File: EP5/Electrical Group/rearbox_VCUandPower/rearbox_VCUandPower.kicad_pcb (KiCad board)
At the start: 2 copper layers, 148.9 x 79.5 mm, 245 parts, among them IC1 MCP6C04T-100E_CHY, IC2 LMR14050SDDAR, IC3 MCP6C04T-100E_CHY, IC4 LD39100PU33RY, IC5 TCAN1057AVDRQ1, IC6 LMR50410Y3FQDBVRQ1, J1 JTAG, J10 24V_raw, J11 24V_raw, J12 5V external, J13 USBC_RPI_5VOnly, J14 USBA_RPI_5Vonly, J15 fan1, J16 fan2, J17 UPS_cap, J18 5Vout, J19 Rpi, J2 MSD-4-A, J20 GPS_UART, J21 3V3out, J22 CAN_termination, J23 CAN, J24 left connector, J25 rear_connector, J26 buzzer, J27 I2C, J3 USB_OTG, J4 LVBattery, J5 GLVMS, J6 GPVMP, J7 24V_noisy1, J8 24V_noisy1, J9 24V_noisy1, Q1 SI3407, SW1 BOOT0, SW2 VBUS, SW3 NRST, U1 STM32H562VGTx, U2 USBLC6-2SC6, U3 LM2903, U4 MAX487E, U5 MAX487E, U6 74HC595, U7 74HC595, U8 SM420561N, U9 SM420561N, Y1 24MHz, Y2 32.768kHz

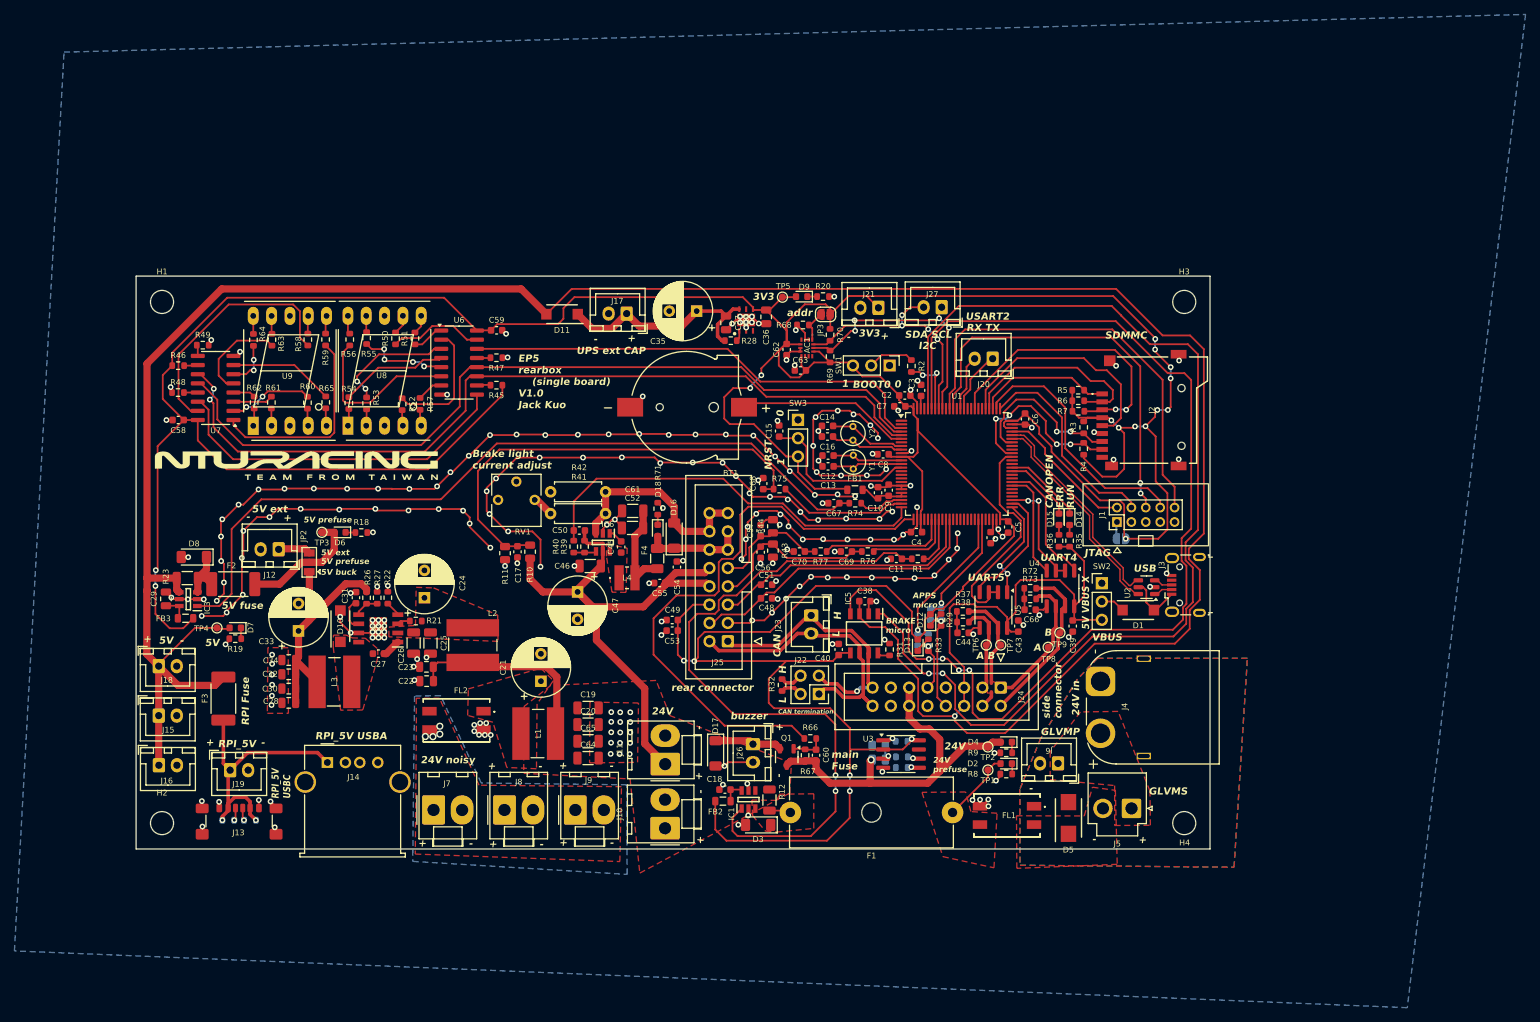
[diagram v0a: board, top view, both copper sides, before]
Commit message: add rearbox_VCUandPower to EP5
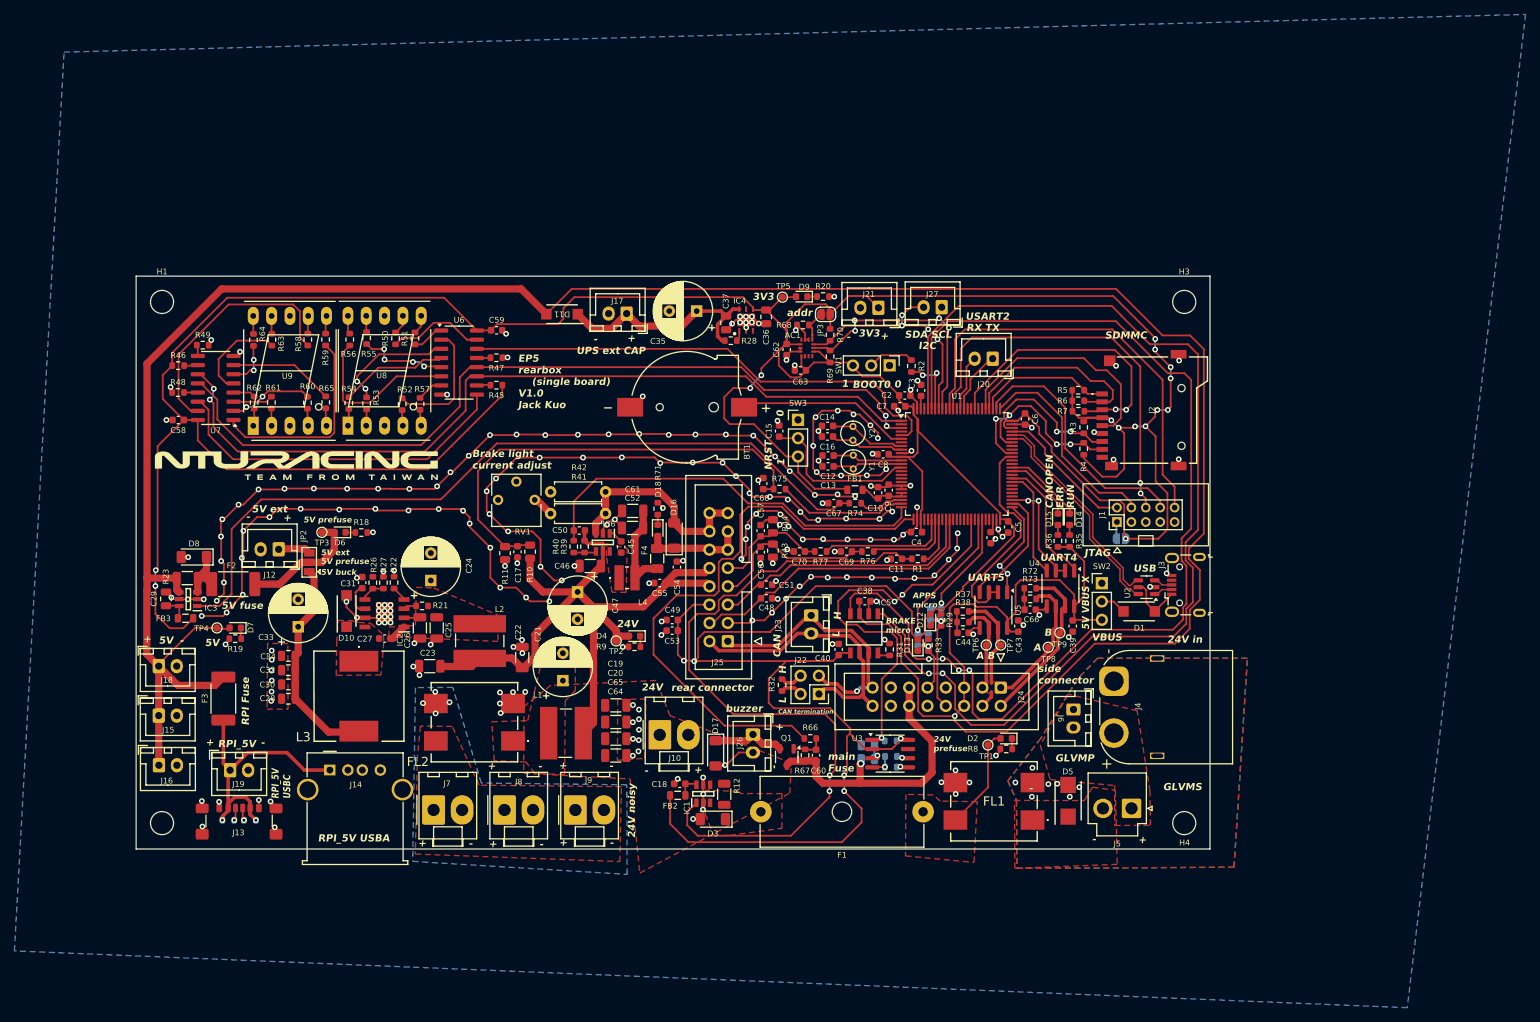
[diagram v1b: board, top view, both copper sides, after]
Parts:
- removed J11: 24V_raw, Connector_Molex:Molex_KK-396_A-41791-0002_1x02_P3.96mm_Vertical
- AC1: value LSM6DSOXTR -> LSM6DSO32
- C1, C3: value 2.2u 16V -> 2u2 16V
- C11, C67, C68, C69, C70: value 0u1 -> 1u
- C19, C20, C64, C65: value 1u 35V -> 10u 35V
- C22, C23: value 1u 35V -> 10u 35V; footprint Capacitor_SMD:C_0805_2012Metric -> Capacitor_SMD:C_1206_3216Metric
- C29: value 1u 16V -> 10u 16V
- D1, D10, D11: value 45V 2A (VSSAF5L45HM3_A_H) -> 45V 3A (VSSAF5L45HM3_A_H)
- F2: value 1A -> 3A
- F4: value 0.5A -> 1A
- FL1, FL2: value SRF0905A-202Y -> ACM12V-351-2PL-TL00; footprint SamacSys_Parts:SRF0905A102Y -> SamacSys_Parts:ACM12V3512PLTL00
- L1: value ?uH 10A () -> 1.5uH 10A (SRP6530A-1R5M)
- L2: value ?uH 1A -> 18uH 1.5A (SRR6040A-180M)
- L3: value 18uF 1A (SRR6040A-180M) -> 22uH 4A (SRR1260A-220M); footprint SamacSys_Parts:SRR6040A180M -> SamacSys_Parts:SRR1260A220M
- R13: value 100k -> 270k
- R43, R44: value 150R 1% -> 120R 1%
- R74, R75, R76, R77: value 1k -> 10k
- moved R9 53.6 mm to (128.3, 106.5)
- moved TP2 53.6 mm to (125.8, 105.7)
- moved D4 53.6 mm to (128.3, 105.0)
- moved C22 13.7 mm to (112.7, 108.0), turned to 90 degrees
- moved J10 13.0 mm to (131.8, 118.7), turned to 0 degrees
- moved J6 7.78 mm to (189.2, 115.2), turned to -90 degrees
- moved D3 6.32 mm to (139.2, 130.4)
- moved IC1 6.32 mm to (137.8, 126.9)
- moved C18 6.32 mm to (134.6, 125.5)
- moved FB2 6.32 mm to (134.3, 127.1)
- moved R12 6.32 mm to (140.7, 126.9)
- moved F1 4.09 mm to (168.3, 129.4)
- moved L3 3.93 mm to (90.1, 113.3), turned to 0 degrees
- moved C19 3.87 mm to (125.7, 114.6)
- moved C65 3.87 mm to (125.7, 119.2)
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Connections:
- net /SCL1_SCL renamed /I2C1_SCL
- net /SCL1_SDA renamed /I2C1_SDA
- FL1 pad 1: GNDPWR -> /power/+24V_preCMfilter
- FL1 pad 2: /power/+24V_preCMfilter -> GNDPWR
- FL1 pad 3: /power/+24V_proCMfilter -> GND
- FL1 pad 4: GND -> /power/+24V_proCMfilter
- U1 pad 1: /SPI4_MISO -> /SPI4_SCK
- U1 pad 3: /SPI4_MOSI -> /SPI4_CS
- U1 pad 4: /SPI4_CS -> /SPI4_MISO
- U1 pad 42: unconnected-(U1-PE11-Pad42) -> /24V_lowTrig
- U1 pad 5: /SPI4_SCK -> /SPI4_MOSI
- U1 pad 57: /UART4_TX -> unconnected-(U1-PD10-Pad57)
- U1 pad 58: /UART4_RX -> /UART4_TX
- U1 pad 59: unconnected-(U1-PD12-Pad59) -> /UART4_RX
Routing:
- net /24V_lowTrig: track 2.01 -> 55.0 mm, vias 1 -> 3
- net GND: track 482.8 -> 522.6 mm
- net +24V: track 159.1 -> 148.8 mm
- net +3V3: track 654.7 -> 664.2 mm
- net /5V_3V3/5V_buck: track 36.1 -> 29.8 mm
- net /power/24V_noisyN: track 5.72 -> 0.00 mm
- net /I_meassure_all: track 97.8 -> 102.7 mm
- net /power/+24V_proCMfilter: track 10.0 -> 14.4 mm
- net /SPI4_MOSI: track 65.3 -> 68.6 mm
- net /power/+24V_premessure: track 3.01 -> 0.00 mm
- net /5V_3V3/24V_5VbuckIn: track 0.00 -> 2.23 mm
- net /SPI4_SCK: track 116.9 -> 115.1 mm
- net /5V_3V3/Rpi_Vbus: track 36.9 -> 37.7 mm
- net /electrical3/buzzer_outbox: track 9.38 -> 10.1 mm
- net /FDCAN1_RX: track 151.9 -> 151.3 mm
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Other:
- board text added: "T_VCC"
